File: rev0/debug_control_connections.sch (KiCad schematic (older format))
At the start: 1 part

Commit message: rev0: finish capture and start routing (woo!)
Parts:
- IC1: renamed from IC?; footprint BGA256C80P16X16_1400X1400X170 -> luna:lattice_cabga256
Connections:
- net labels added: +3V3
- no-connect marks 0 -> 17
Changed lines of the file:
@@
 $Descr A4 11693 8268
 encoding utf-8
-Sheet 8 9
+Sheet 7 9
 Title "LUNA: Debug and Control Connections"
 Date "2019-10-20"
@@
 SUPPLY_POWER_TO_TARGET
 $Comp
-L fpgas_and_processors:ECP5-BGA256 IC?
+L fpgas_and_processors:ECP5-BGA256 IC1
 U 2 1 5DFF5299
 P 2200 1950
-F 0 "IC?" H 2170 508 50  0000 R CNN
+F 0 "IC1" H 2170 508 50  0000 R CNN
 F 1 "ECP5-BGA256" H 2170 418 50  0000 R CNN
-F 2 "BGA256C80P16X16_1400X1400X170" H -1000 5400 50  0001 L CNN
+F 2 "luna:lattice_cabga256" H -1000 5400 50  0001 L CNN
 F 3 "" H -1450 6350 50  0001 L CNN
 F 4 "FPGA - Field Programmable Gate Array ECP5; 12k LUTs; 1.1V" H -1450 6250 50  0001 L CNN "Description"
@@
 Text HLabel 3600 4750 2    50   Input ~ 0
 CLKIN_60MHZ
+NoConn ~ 3150 2500
+NoConn ~ 3150 2800
+NoConn ~ 3150 2900
+NoConn ~ 3150 3000
+NoConn ~ 3150 3100
+NoConn ~ 3150 3200
+NoConn ~ 3150 3300
+NoConn ~ 3150 3400
+NoConn ~ 3150 3500
+NoConn ~ 3150 3850
+NoConn ~ 3150 3950
+NoConn ~ 3150 4050
+NoConn ~ 3150 4150
+NoConn ~ 3150 4250
+NoConn ~ 3150 4350
+NoConn ~ 3150 4450
+NoConn ~ 3150 4550
+$Comp
+L power:+3V3 #PWR0105
+U 1 1 5E3ECE52
+P 2450 1500
+F 0 "#PWR0105" H 2450 1350 50  0001 C CNN
+F 1 "+3V3" H 2464 1673 50  0000 C CNN
+F 2 "" H 2450 1500 50  0001 C CNN
+F 3 "" H 2450 1500 50  0001 C CNN
+	1    2450 1500
+	1    0    0    -1
+$EndComp
 $EndSCHEMATC

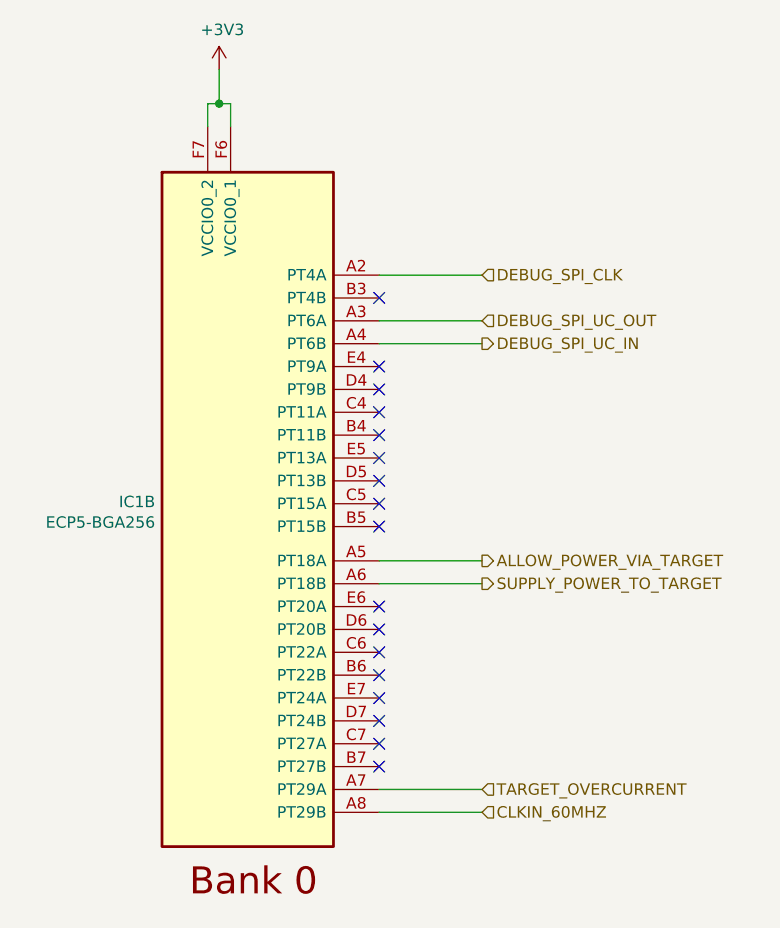
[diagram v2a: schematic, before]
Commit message: rev0: get most of the major routing done
still needs power routing, length matching for the busses,
and routing for the misc control stuff
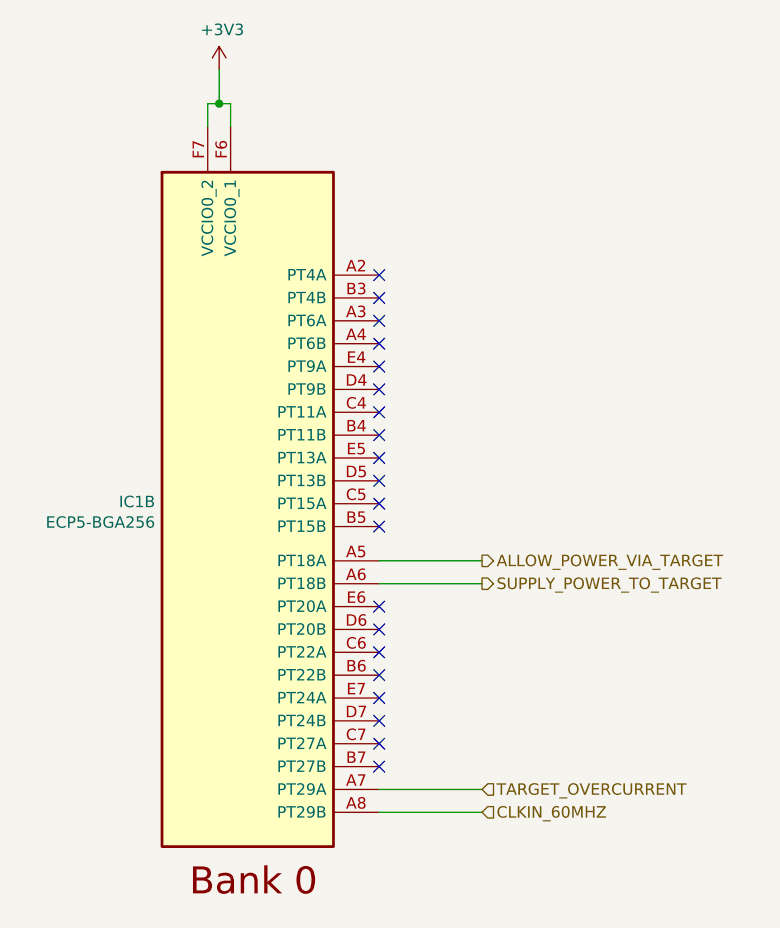
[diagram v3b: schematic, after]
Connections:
- net DEBUG_SPI_CLK: no longer names the net of IC1.A2 (PT4A)
- net DEBUG_SPI_UC_IN: no longer names the net of IC1.A4 (PT6B)
- net DEBUG_SPI_UC_OUT: no longer names the net of IC1.A3 (PT6A)
- no-connect marks 17 -> 20
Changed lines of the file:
@@
 	2450 1650 2500 1650
-Wire Wire Line
-	3150 2400 3600 2400
-Wire Wire Line
-	3150 2600 3600 2600
-Wire Wire Line
-	3150 2700 3600 2700
 Wire Wire Line
 	3150 3650 3600 3650
@@
 Wire Wire Line
 	3150 4750 3600 4750
-Text HLabel 3600 2600 2    50   Input ~ 0
-DEBUG_SPI_UC_OUT
-Text HLabel 3600 2700 2    50   Output ~ 0
-DEBUG_SPI_UC_IN
-Text HLabel 3600 2400 2    50   Input ~ 0
-DEBUG_SPI_CLK
 Text HLabel 3600 3650 2    50   Output ~ 0
 ALLOW_POWER_VIA_TARGET
@@
 	1    0    0    -1
 $EndComp
+NoConn ~ 3150 2400
+NoConn ~ 3150 2600
+NoConn ~ 3150 2700
 $EndSCHEMATC

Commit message: rev0: implement all of the routing except length matching
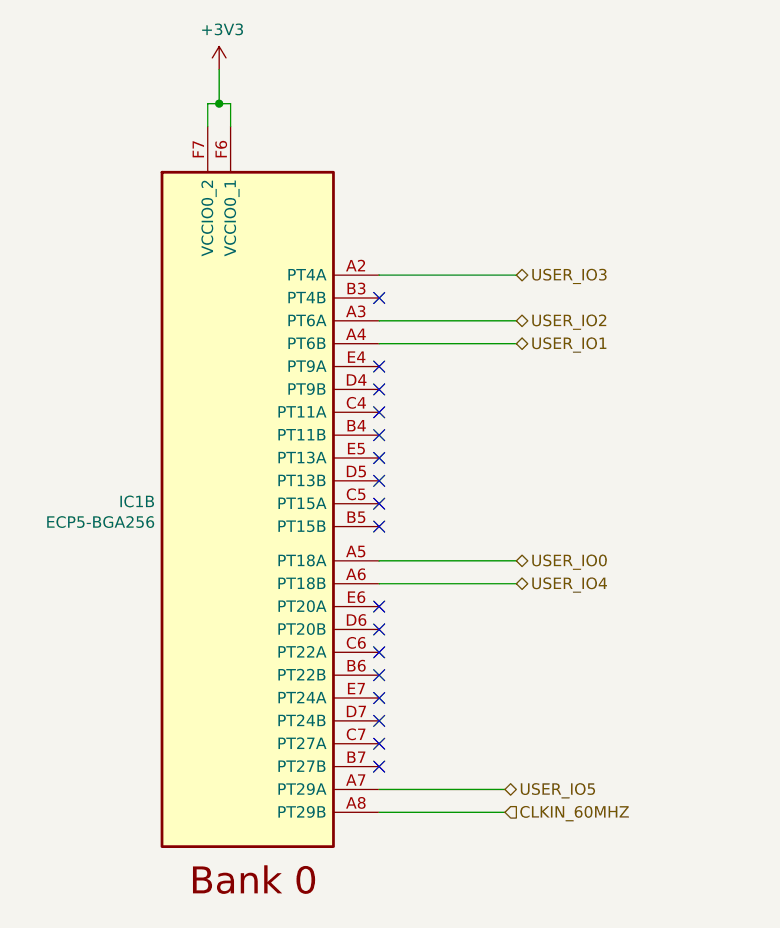
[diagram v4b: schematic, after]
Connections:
- net USER_IO3: now reaches IC1.A2 (PT4A)
- net USER_IO2: now reaches IC1.A3 (PT6A)
- net USER_IO1: now reaches IC1.A4 (PT6B)
- net ALLOW_POWER_VIA_TARGET renamed USER_IO0
- net SUPPLY_POWER_TO_TARGET renamed USER_IO4
- net TARGET_OVERCURRENT renamed USER_IO5
- no-connect marks 20 -> 17
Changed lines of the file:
@@
 $Descr A4 11693 8268
 encoding utf-8
-Sheet 7 9
+Sheet 9 9
 Title "LUNA: Debug and Control Connections"
 Date "2019-10-20"
@@
 Wire Wire Line
 	2450 1650 2500 1650
-Wire Wire Line
-	3150 3650 3600 3650
-Wire Wire Line
-	3150 3750 3600 3750
-Wire Wire Line
-	3150 4650 3600 4650
-Wire Wire Line
-	3150 4750 3600 4750
-Text HLabel 3600 3650 2    50   Output ~ 0
-ALLOW_POWER_VIA_TARGET
-Text HLabel 3600 3750 2    50   Output ~ 0
-SUPPLY_POWER_TO_TARGET
 $Comp
 L fpgas_and_processors:ECP5-BGA256 IC1
@@
 	1    0    0    -1
 $EndComp
-Text HLabel 3600 4650 2    50   Input ~ 0
-TARGET_OVERCURRENT
-Text HLabel 3600 4750 2    50   Input ~ 0
+Text HLabel 3700 4750 2    50   Input ~ 0
 CLKIN_60MHZ
 NoConn ~ 3150 2500
@@
 	1    0    0    -1
 $EndComp
-NoConn ~ 3150 2400
-NoConn ~ 3150 2600
-NoConn ~ 3150 2700
+Wire Wire Line
+	3150 2400 3750 2400
+Wire Wire Line
+	3150 2600 3750 2600
+Wire Wire Line
+	3150 2700 3750 2700
+Wire Wire Line
+	3150 3650 3750 3650
+Wire Wire Line
+	3150 3750 3750 3750
+Text HLabel 3750 3650 2    50   BiDi ~ 0
+USER_IO0
+Text HLabel 3750 2700 2    50   BiDi ~ 0
+USER_IO1
+Text HLabel 3750 2600 2    50   BiDi ~ 0
+USER_IO2
+Text HLabel 3750 2400 2    50   BiDi ~ 0
+USER_IO3
+Text HLabel 3750 3750 2    50   BiDi ~ 0
+USER_IO4
+Wire Wire Line
+	3150 4650 3700 4650
+Text HLabel 3700 4650 2    50   BiDi ~ 0
+USER_IO5
+Wire Wire Line
+	3150 4750 3700 4750
 $EndSCHEMATC

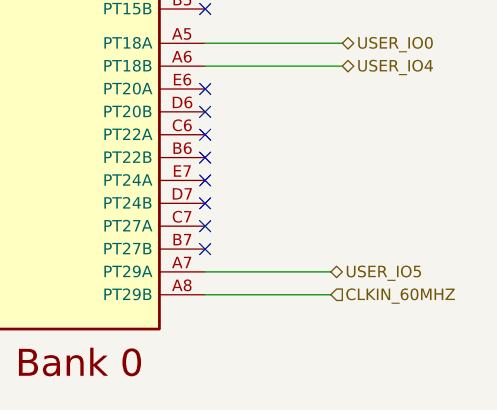
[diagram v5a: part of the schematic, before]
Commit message: pre r0.2 -- minor improvements and debug fixes
- add silkscreen connector diagrams
- added test points for clock and voltage rails
- moved SPI connectors for reduced via density (DFM)
- added chip select for debug SPI
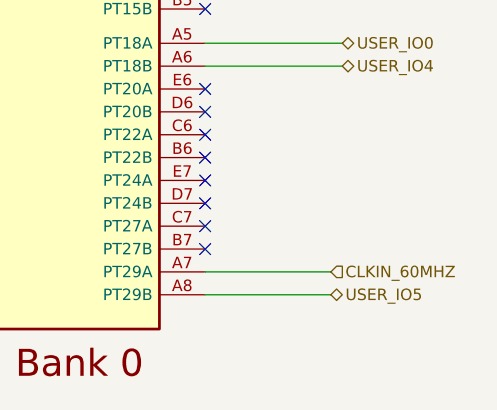
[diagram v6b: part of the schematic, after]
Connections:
- net CLKIN_60MHZ: now also IC1.A7 (PT29A); no longer IC1.A8 (PT29B)
- net USER_IO5: now also IC1.A8 (PT29B); no longer IC1.A7 (PT29A)
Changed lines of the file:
@@
 	1    0    0    -1
 $EndComp
-Text HLabel 3700 4750 2    50   Input ~ 0
+Text HLabel 3700 4650 2    50   Input ~ 0
 CLKIN_60MHZ
 NoConn ~ 3150 2500
@@
 USER_IO4
 Wire Wire Line
-	3150 4650 3700 4650
-Text HLabel 3700 4650 2    50   BiDi ~ 0
+	3150 4750 3700 4750
+Text HLabel 3700 4750 2    50   BiDi ~ 0
 USER_IO5
 Wire Wire Line
-	3150 4750 3700 4750
+	3150 4650 3700 4650
 $EndSCHEMATC
